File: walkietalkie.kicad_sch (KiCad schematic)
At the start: 12 parts, among them J1 Conn_01x05_Pin, J2 Conn_01x02_Pin, J3 Conn_01x02_Pin, SW1 PTT, U2 NRF24L01_Breakout, U7 ER_OLEDM0.91_1x-I2C

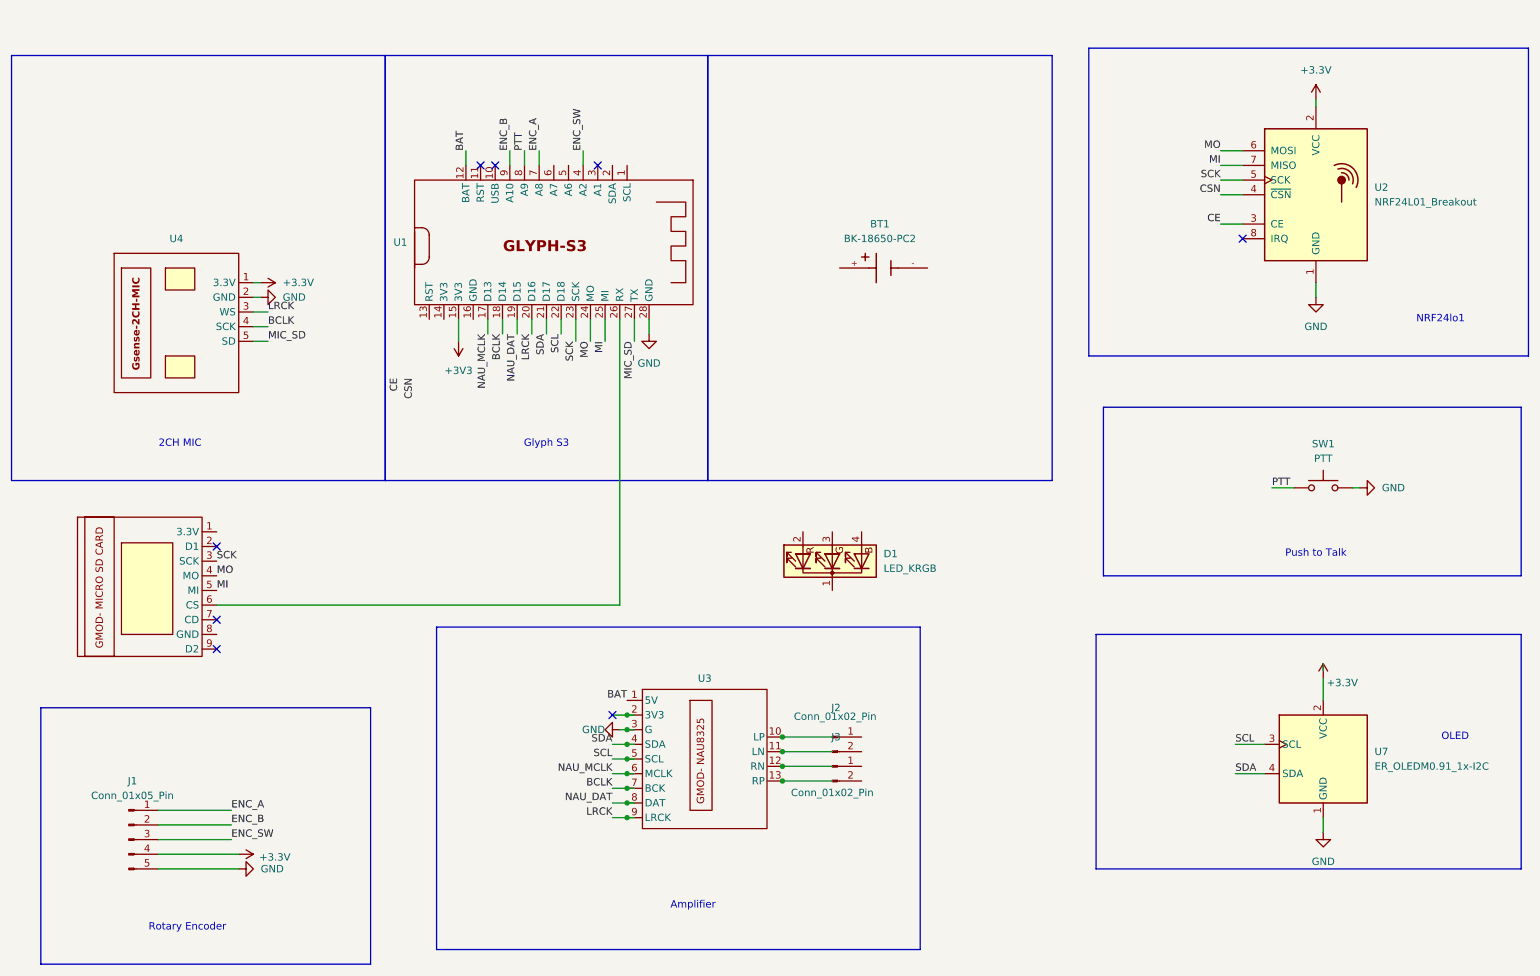
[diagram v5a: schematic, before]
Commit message: feat: routing almost done, GND and VCC remaining
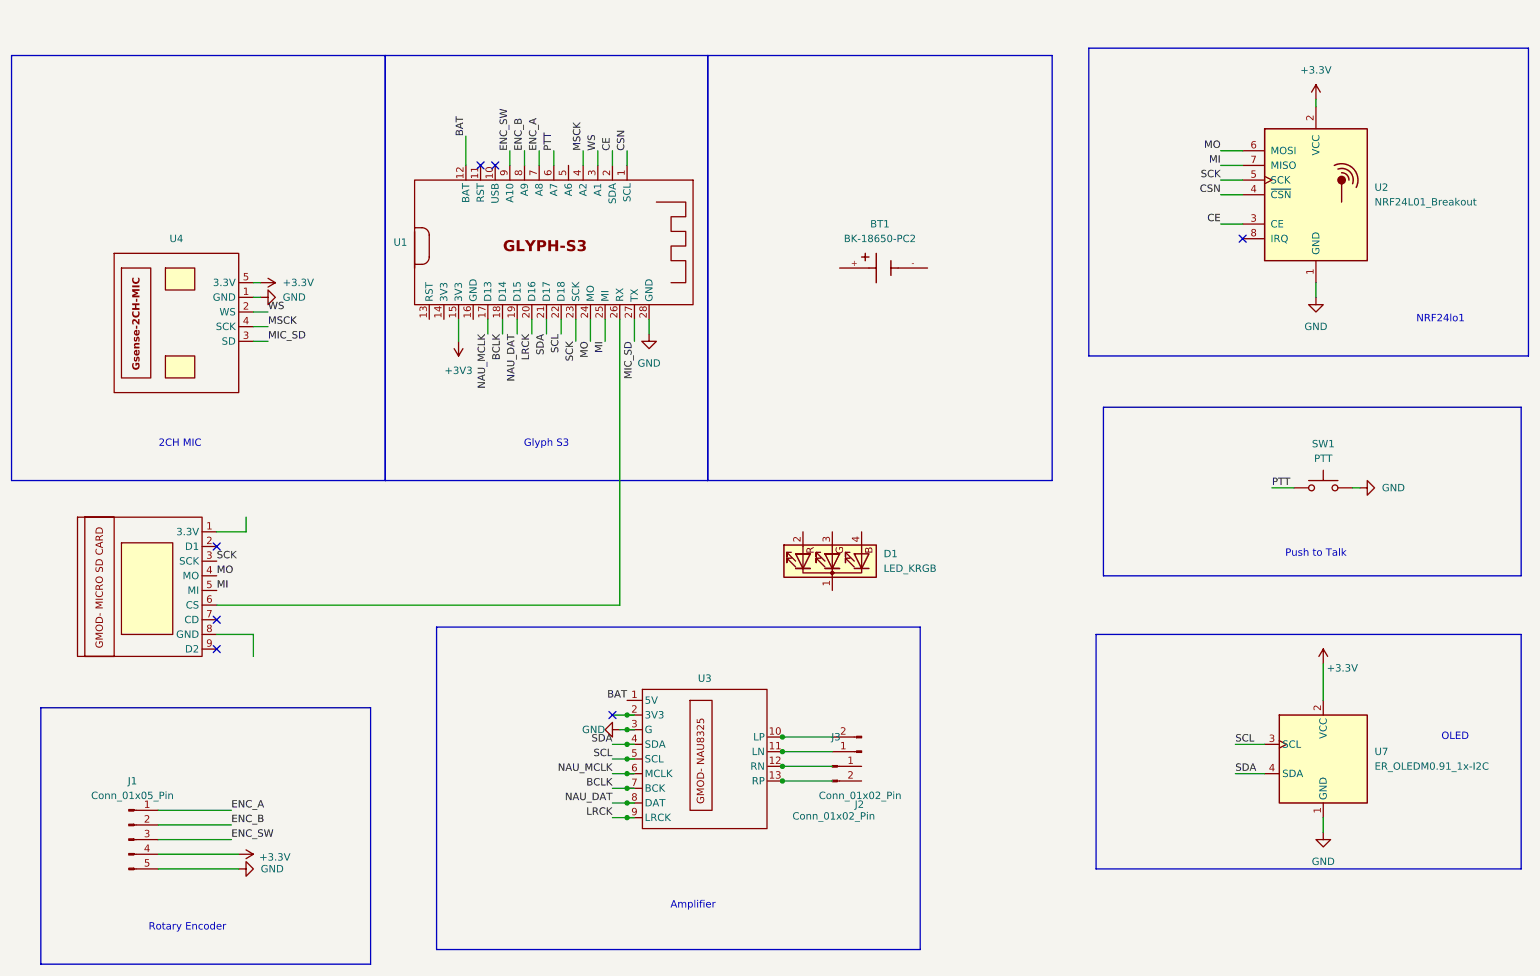
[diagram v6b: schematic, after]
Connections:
- net +3.3V: now also U4.5 (3.3V); no longer U4.1 (3.3V)
- net BCLK: no longer U4.4 (SCK)
- net CE: now also U1.2 (SDA)
- net CSN: now also U1.1 (SCL)
- net ENC_B: now also U1.8 (A9); no longer U1.9 (A10)
- net ENC_SW: now also U1.9 (A10); no longer U1.4 (A2)
- net GND: now also U4.1 (GND); no longer U4.2 (GND)
- net LRCK: no longer U4.3 (WS)
- net MIC_SD: now also U4.3 (SD); no longer U4.5 (SD)
- net PTT: now also U1.6 (A7); no longer U1.8 (A9)
- net WS: now reaches U1.3 (A1)
- net WS: now also U4.2 (WS)
- net at U3.10 (LP): now also J2.2 (Pin_2)
- net at U3.11 (LN): now also J2.1 (Pin_1)
- new net MSCK: U1.4 (A2), U4.4 (SCK)
- no-connect marks 8 -> 7
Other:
- moved on the sheet: J2

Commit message: fix: resolve schematic problems
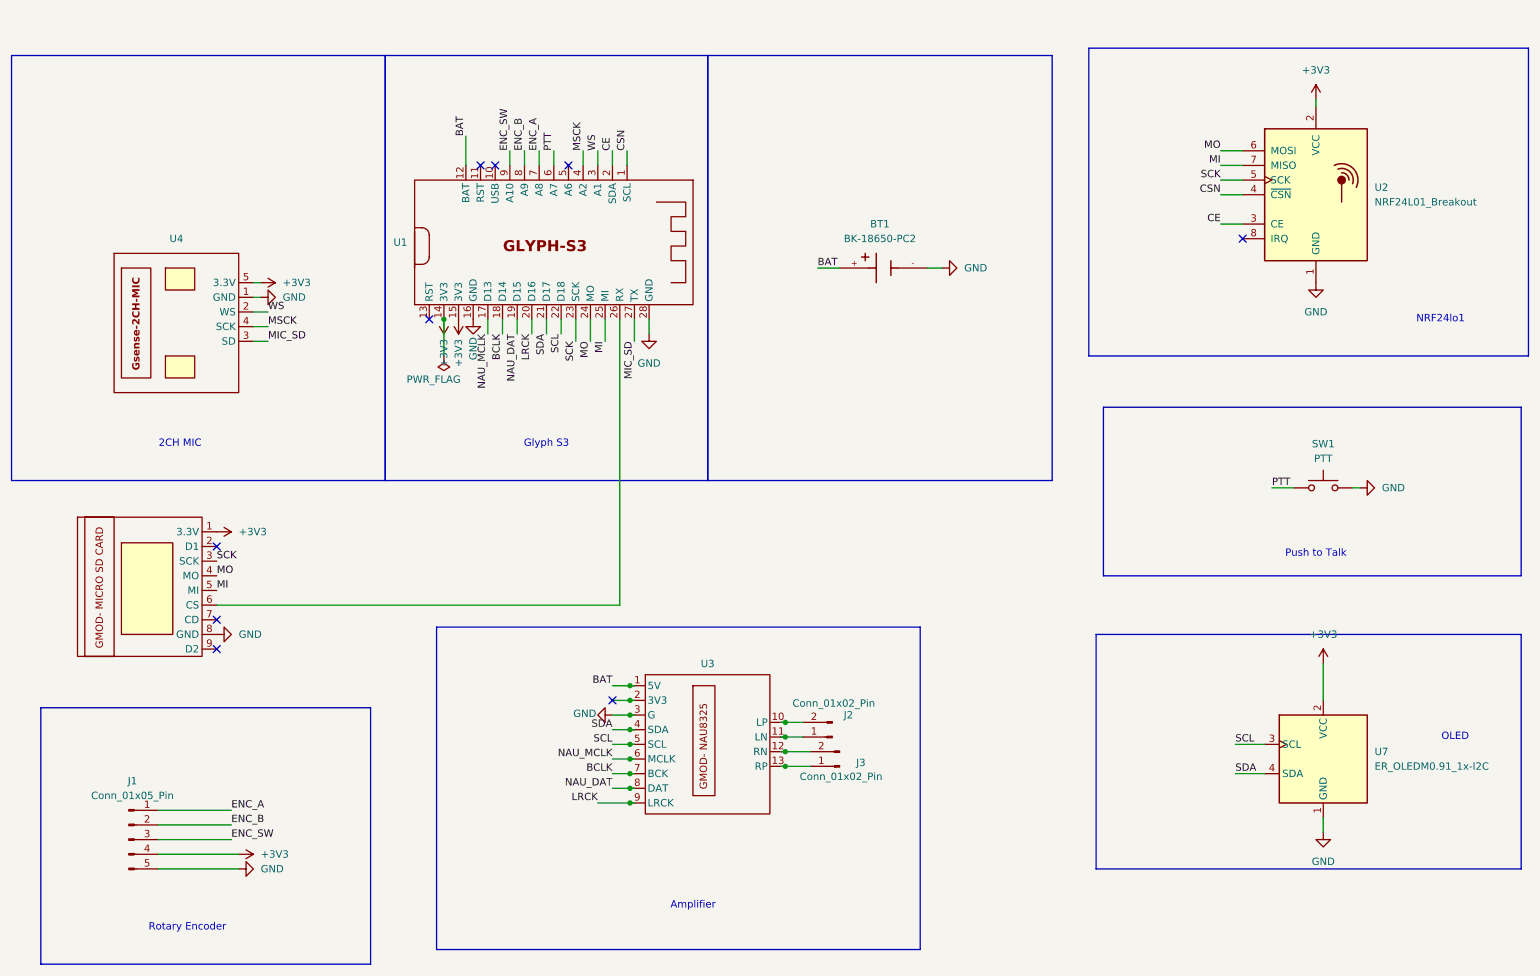
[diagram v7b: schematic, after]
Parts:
- removed D1: LED_KRGB, LED_THT:LED_D5.0mm-4_RGB, symbol Device:LED_KRGB
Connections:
- net +3.3V is gone; now on net +3V3: J1.4 (Pin_4), U2.2 (VCC), U4.5 (3.3V), U7.2 (VCC)
- net +3V3: now also U1.14 (3V3), U5.1 (3.3V)
- net BAT: now also BT1.+
- net GND: now also BT1.-, U1.16 (GND), U5.8 (GND)
- net at U3.12 (RN): now also J3.2 (Pin_2)
- net at U3.13 (RP): now also J3.1 (Pin_1)
- no-connect marks 7 -> 9
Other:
- moved on the sheet: J2, J3, U3
